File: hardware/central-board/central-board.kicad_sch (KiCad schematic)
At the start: 64 parts, among them J1 MTJ-88ARX1-FSM-LG, J10 Conn_01x02, J11 Conn_01x02, J12 IO I2C Bus, J2 1729128, J3 1729128, J4 RPi_GPIO, J5 PEC11R, J6 IO Power Bus, J7 GPIO Bus, J8 Conn_01x02, Q1 AO3400A, Q2 AO3400A, Q3 AO3400A, Q4 AO3400A, Q5 AO3400A, Q6 AO3400A, U1 MAX3485, U4 TPS5430DDAR, U5 XC6220B331MR, U6 TPS5430DDAR

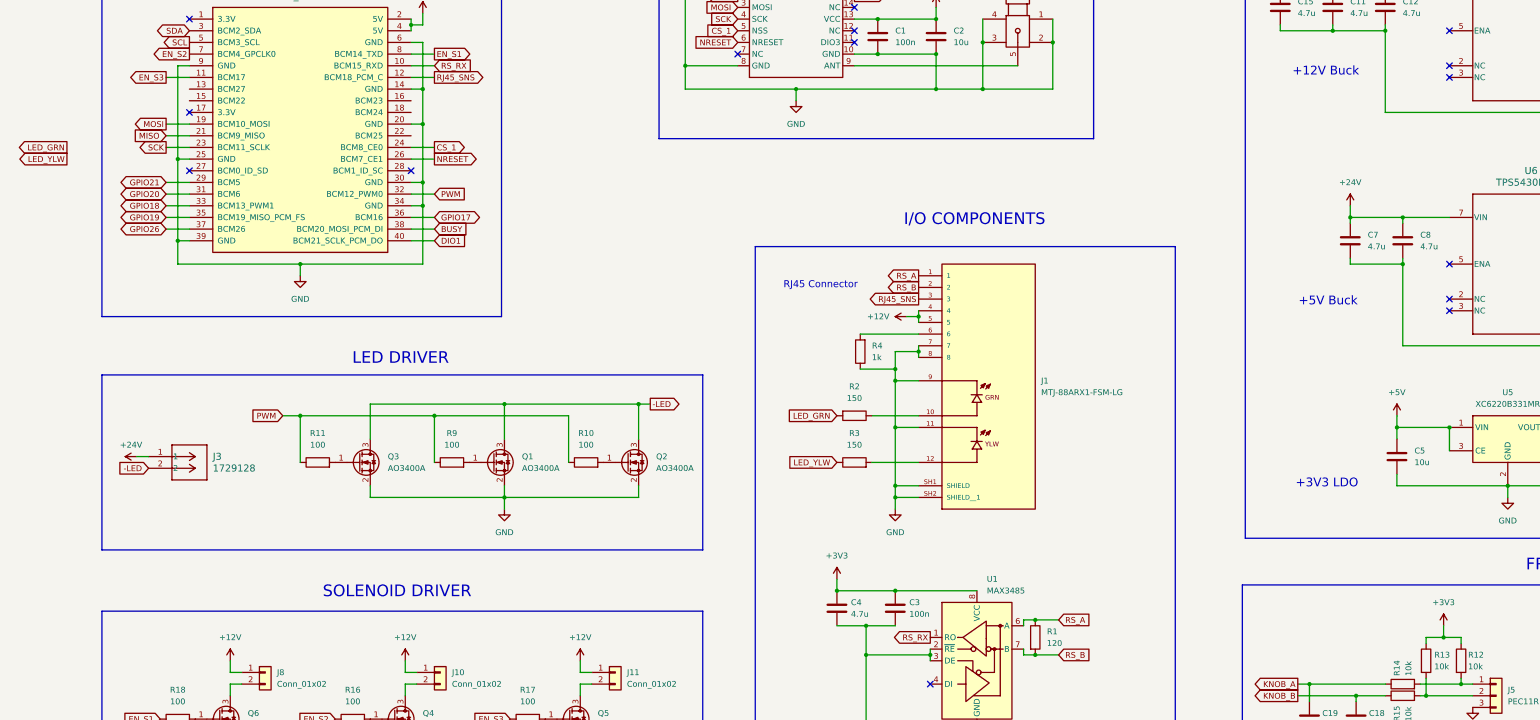
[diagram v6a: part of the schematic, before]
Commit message: All primary components mounted
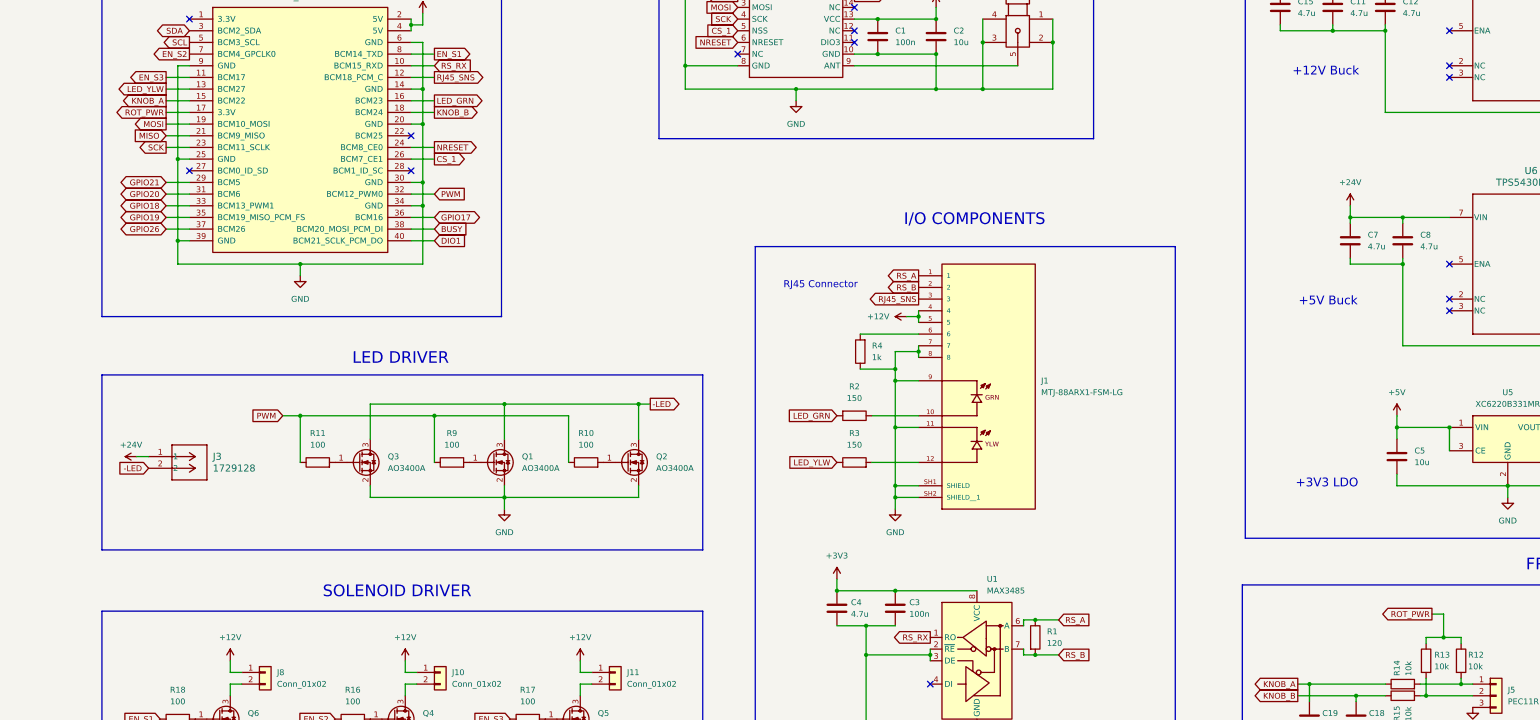
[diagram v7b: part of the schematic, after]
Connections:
- net +3V3: no longer R12.1, R13.1
- net CS_1: now also J4.26 (BCM7_CE1); no longer J4.24 (BCM8_CE0)
- net KNOB_A: now also J4.15 (BCM22)
- net KNOB_B: now also J4.18 (BCM24)
- net LED_GRN: now also J4.16 (BCM23)
- net LED_YLW: now also J4.13 (BCM27)
- net NRESET: now also J4.24 (BCM8_CE0); no longer J4.26 (BCM7_CE1)
- net ROT_PWR: now reaches J4.17 (3.3V)
- net ROT_PWR: now also R12.1, R13.1
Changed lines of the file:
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@@
 	)
 	(no_connect
-		(at 113.03 147.32)
-	)
-	(no_connect
 		(at 257.81 132.08)
 	)
@@
 	)
 	(no_connect
+		(at 161.29 152.4)
+	)
+	(no_connect
 		(at 113.03 160.02)
 	)
@@
 	(wire
 		(pts
+			(xy 107.95 147.32) (xy 113.03 147.32)
+		)
+		(stroke
+			(width 0)
+			(type default)
+		)
+	)
+	(wire
+		(pts
 			(xy 166.37 172.72) (xy 161.29 172.72)
 		)
@@
 	(wire
 		(pts
+			(xy 166.37 147.32) (xy 161.29 147.32)
+		)
+		(stroke
+			(width 0)
+			(type default)
+		)
+	)
+	(wire
+		(pts
 			(xy 200.66 271.78) (xy 198.12 271.78)
 		)
@@
 	(wire
 		(pts
-			(xy 447.04 127) (xy 462.28 127)
+			(xy 383.54 256.54) (xy 386.08 256.54)
 		)
 		(stroke
@@
 	(wire
 		(pts
-			(xy 271.78 191.77) (xy 271.78 193.04)
+			(xy 447.04 127) (xy 462.28 127)
 		)
 		(stroke
@@
 	(wire
 		(pts
-			(xy 447.04 128.27) (xy 447.04 127)
+			(xy 271.78 191.77) (xy 271.78 193.04)
 		)
 		(stroke
@@
 	(wire
 		(pts
-			(xy 386.08 259.08) (xy 386.08 261.62)
+			(xy 447.04 128.27) (xy 447.04 127)
 		)
 		(stroke
@@
 	(wire
 		(pts
+			(xy 107.95 144.78) (xy 113.03 144.78)
+		)
+		(stroke
+			(width 0)
+			(type default)
+		)
+	)
+	(wire
+		(pts
 			(xy 261.62 223.52) (xy 271.78 223.52)
 		)
@@
 	(wire
 		(pts
-			(xy 166.37 154.94) (xy 161.29 154.94)
-		)
-		(stroke
-			(width 0)
-			(type default)
-		)
-	)
-	(wire
-		(pts
 			(xy 181.61 210.82) (xy 181.61 218.44)
 		)
@@
 	(wire
 		(pts
+			(xy 166.37 144.78) (xy 161.29 144.78)
+		)
+		(stroke
+			(width 0)
+			(type default)
+		)
+	)
+	(wire
+		(pts
 			(xy 124.46 271.78) (xy 121.92 271.78)
 		)
@@
 	(wire
 		(pts
+			(xy 386.08 256.54) (xy 386.08 261.62)
+		)
+		(stroke
+			(width 0)
+			(type default)
+		)
+	)
+	(wire
+		(pts
 			(xy 354.33 274.32) (xy 367.03 274.32)
 		)
@@
 	(wire
 		(pts
-			(xy 166.37 157.48) (xy 161.29 157.48)
+			(xy 107.95 165.1) (xy 113.03 165.1)
 		)
 		(stroke
@@
 	(wire
 		(pts
-			(xy 107.95 165.1) (xy 113.03 165.1)
+			(xy 166.37 213.36) (xy 195.58 213.36)
 		)
 		(stroke
@@
 	(wire
 		(pts
-			(xy 166.37 213.36) (xy 195.58 213.36)
+			(xy 473.71 147.32) (xy 462.28 147.32)
 		)
 		(stroke
@@
 	(wire
 		(pts
-			(xy 473.71 147.32) (xy 462.28 147.32)
+			(xy 454.66 265.43) (xy 457.2 265.43)
 		)
 		(stroke
@@
 	(wire
 		(pts
-			(xy 454.66 265.43) (xy 457.2 265.43)
+			(xy 161.29 128.27) (xy 161.29 129.54)
 		)
 		(stroke
@@
 	(wire
 		(pts
-			(xy 161.29 128.27) (xy 161.29 129.54)
+			(xy 166.37 154.94) (xy 161.29 154.94)
 		)
 		(stroke
@@
 	(wire
 		(pts
+			(xy 166.37 157.48) (xy 161.29 157.48)
+		)
+		(stroke
+			(width 0)
+			(type default)
+		)
+	)
+	(wire
+		(pts
 			(xy 257.81 127) (xy 262.89 127)
 		)
@@
 	(wire
 		(pts
+			(xy 107.95 142.24) (xy 113.03 142.24)
+		)
+		(stroke
+			(width 0)
+			(type default)
+		)
+	)
+	(wire
+		(pts
 			(xy 274.32 265.43) (xy 274.32 266.7)
 		)
@@
 		)
 	)
+	(global_label "ROT_PWR"
+		(shape output)
+		(at 107.95 147.32 180)
+		(fields_autoplaced yes)
+		(effects
+			(font
+				(size 1.27 1.27)
+			)
+			(justify right)
+		)
+		(property "Intersheetrefs" "${INTERSHEET_REFS}"
+			(at 96.4377 147.32 0)
+			(effects
+				(font
+					(size 1.27 1.27)
+				)
+				(justify right)
+				(hide yes)
+			)
+		)
+	)
 	(global_label "EN_S1"
 		(shape output)
@@
 		)
 	)
+	(global_label "ROT_PWR"
+		(shape output)
+		(at 383.54 256.54 180)
+		(fields_autoplaced yes)
+		(effects
+			(font
+				(size 1.27 1.27)
+			)
+			(justify right)
+		)
+		(property "Intersheetrefs" "${INTERSHEET_REFS}"
+			(at 372.0277 256.54 0)
+			(effects
+				(font
+					(size 1.27 1.27)
+				)
+				(justify right)
+				(hide yes)
+			)
+		)
+	)
 	(global_label "GPIO17"
 		(shape bidirectional)
@@
 		)
 	)
+	(global_label "KNOB_A"
+		(shape output)
+		(at 107.95 144.78 180)
+		(fields_autoplaced yes)
+		(effects
+			(font
+				(size 1.27 1.27)
+			)
+			(justify right)
+		)
+		(property "Intersheetrefs" "${INTERSHEET_REFS}"
+			(at 97.7076 144.78 0)
+			(effects
+				(font
+					(size 1.27 1.27)
+				)
+				(justify right)
+				(hide yes)
+			)
+		)
+	)
 	(global_label "NRESET"
 		(shape input)
@@
 	(global_label "LED_YLW"
 		(shape output)
-		(at 86.36 157.48 180)
+		(at 107.95 142.24 180)
 		(fields_autoplaced yes)
 		(effects
@@
 		)
 		(property "Intersheetrefs" "${INTERSHEET_REFS}"
-			(at 75.392 157.48 0)
+			(at 96.982 142.24 0)
 			(effects
 				(font
@@
 	(global_label "CS_1"
 		(shape output)
-		(at 166.37 154.94 0)
+		(at 166.37 157.48 0)
 		(fields_autoplaced yes)
 		(effects
@@
 		)
 		(property "Intersheetrefs" "${INTERSHEET_REFS}"
-			(at 174.0118 154.94 0)
+			(at 174.0118 157.48 0)
 			(effects
 				(font
@@
 	(global_label "NRESET"
 		(shape output)
-		(at 166.37 157.48 0)
+		(at 166.37 154.94 0)
 		(fields_autoplaced yes)
 		(effects
@@
 		)
 		(property "Intersheetrefs" "${INTERSHEET_REFS}"
-			(at 176.4308 157.48 0)
+			(at 176.4308 154.94 0)
 			(effects
 				(font
@@
 		)
 	)
+	(global_label "KNOB_B"
+		(shape output)
+		(at 166.37 147.32 0)
+		(fields_autoplaced yes)
+		(effects
+			(font
+				(size 1.27 1.27)
+			)
+			(justify left)
+		)
+		(property "Intersheetrefs" "${INTERSHEET_REFS}"
+			(at 176.7938 147.32 0)
+			(effects
+				(font
+					(size 1.27 1.27)
+				)
+				(justify left)
+				(hide yes)
+			)
+		)
+	)
 	(global_label "PWM"
 		(shape input)
@@
 	(global_label "LED_GRN"
 		(shape output)
-		(at 86.36 154.94 180)
+		(at 166.37 144.78 0)
 		(fields_autoplaced yes)
 		(effects
@@
 				(size 1.27 1.27)
 			)
-			(justify right)
+			(justify left)
 		)
 		(property "Intersheetrefs" "${INTERSHEET_REFS}"
-			(at 75.0896 154.94 0)
+			(at 177.6404 144.78 0)
 			(effects
 				(font
 					(size 1.27 1.27)
 				)
-				(justify right)
+				(justify left)
 				(hide yes)
 			)
@@
 					(unit 1)
 				)
-			)
-		)
-	)
-	(symbol
-		(lib_id "power:+3V3")
-		(at 386.08 259.08 0)
-		(unit 1)
-		(exclude_from_sim no)
-		(in_bom yes)
-		(on_board yes)
-		(dnp no)
-		(fields_autoplaced yes)
-		(property "Reference" "#PWR022"
-			(at 386.08 262.89 0)
-			(effects
-				(font
-					(size 1.27 1.27)
-				)
-				(hide yes)
-			)
-		)
-		(property "Value" "+3V3"
-			(at 386.08 254 0)
-			(effects
-				(font
-					(size 1.27 1.27)
-				)
-			)
-		)
-		(property "Footprint" ""
-			(at 386.08 259.08 0)
-			(effects
-				(font
-					(size 1.27 1.27)
-				)
-				(hide yes)
-			)
-		)
-		(property "Datasheet" ""
-			(at 386.08 259.08 0)
-			(effects
-				(font
-					(size 1.27 1.27)
-				)
-				(hide yes)
-			)
-		)
-		(property "Description" "Power symbol creates a global label with name \"+3V3\""
-			(at 386.08 259.08 0)
-			(effects
-				(font
-					(size 1.27 1.27)
-				)
-				(hide yes)
-			)
-		)
-		(pin "1"
-		)
-		(instances
-			(project ""
-				(path "/9c3534ca-d5b4-48b7-bfc3-bcc5b38635ff"
-					(reference "#PWR022")
-					(unit 1)
-				)

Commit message: Primary prepared for order
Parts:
- C14, C16, C17: footprint Capacitor_Tantalum_SMD:CP_EIA-7343-15_Kemet-W -> Library2:CAP-SMD_L3.5-W2.8-R-RD
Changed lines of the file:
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@@
 			)
 		)
-		(property "Footprint" "Capacitor_Tantalum_SMD:CP_EIA-7343-15_Kemet-W"
+		(property "Footprint" "Library2:CAP-SMD_L3.5-W2.8-R-RD"
 			(at 474.6752 139.7 0)
 			(effects
@@
 			)
 		)
-		(property "Footprint" "Capacitor_Tantalum_SMD:CP_EIA-7343-15_Kemet-W"
+		(property "Footprint" "Library2:CAP-SMD_L3.5-W2.8-R-RD"
 			(at 486.1052 139.7 0)
 			(effects
@@
 			)
 		)
-		(property "Footprint" "Capacitor_Tantalum_SMD:CP_EIA-7343-15_Kemet-W"
+		(property "Footprint" "Library2:CAP-SMD_L3.5-W2.8-R-RD"
 			(at 463.2452 139.7 0)
 			(effects
